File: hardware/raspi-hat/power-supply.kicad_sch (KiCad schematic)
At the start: 3 parts, among them J3 ATX-20, J4 Raspberry_Pi_4

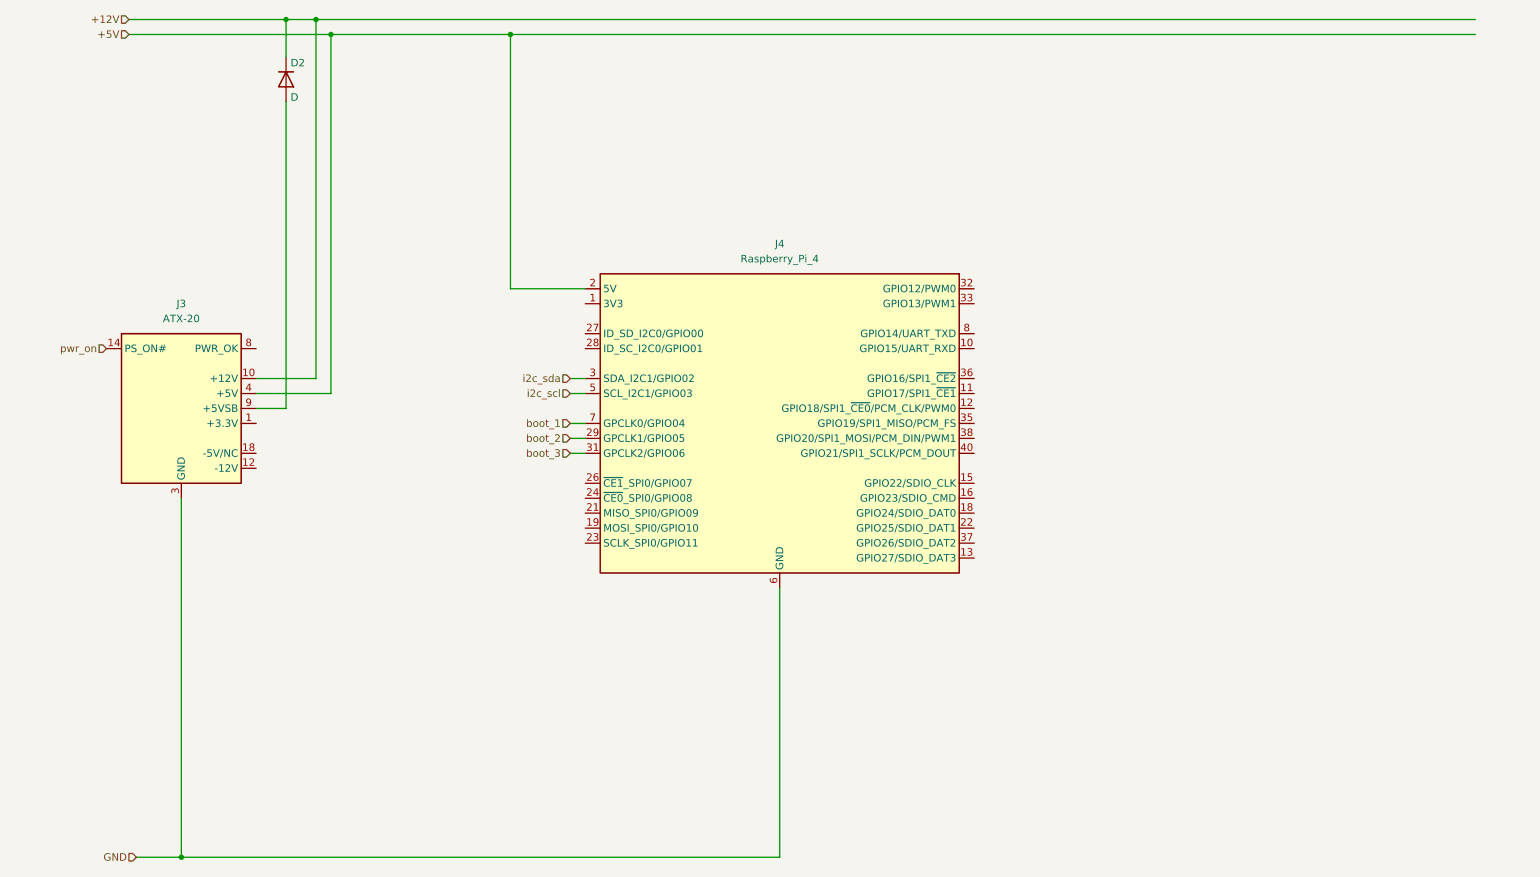
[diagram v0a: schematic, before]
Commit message: - added some lines on hardwaer - added libmotor as dependency
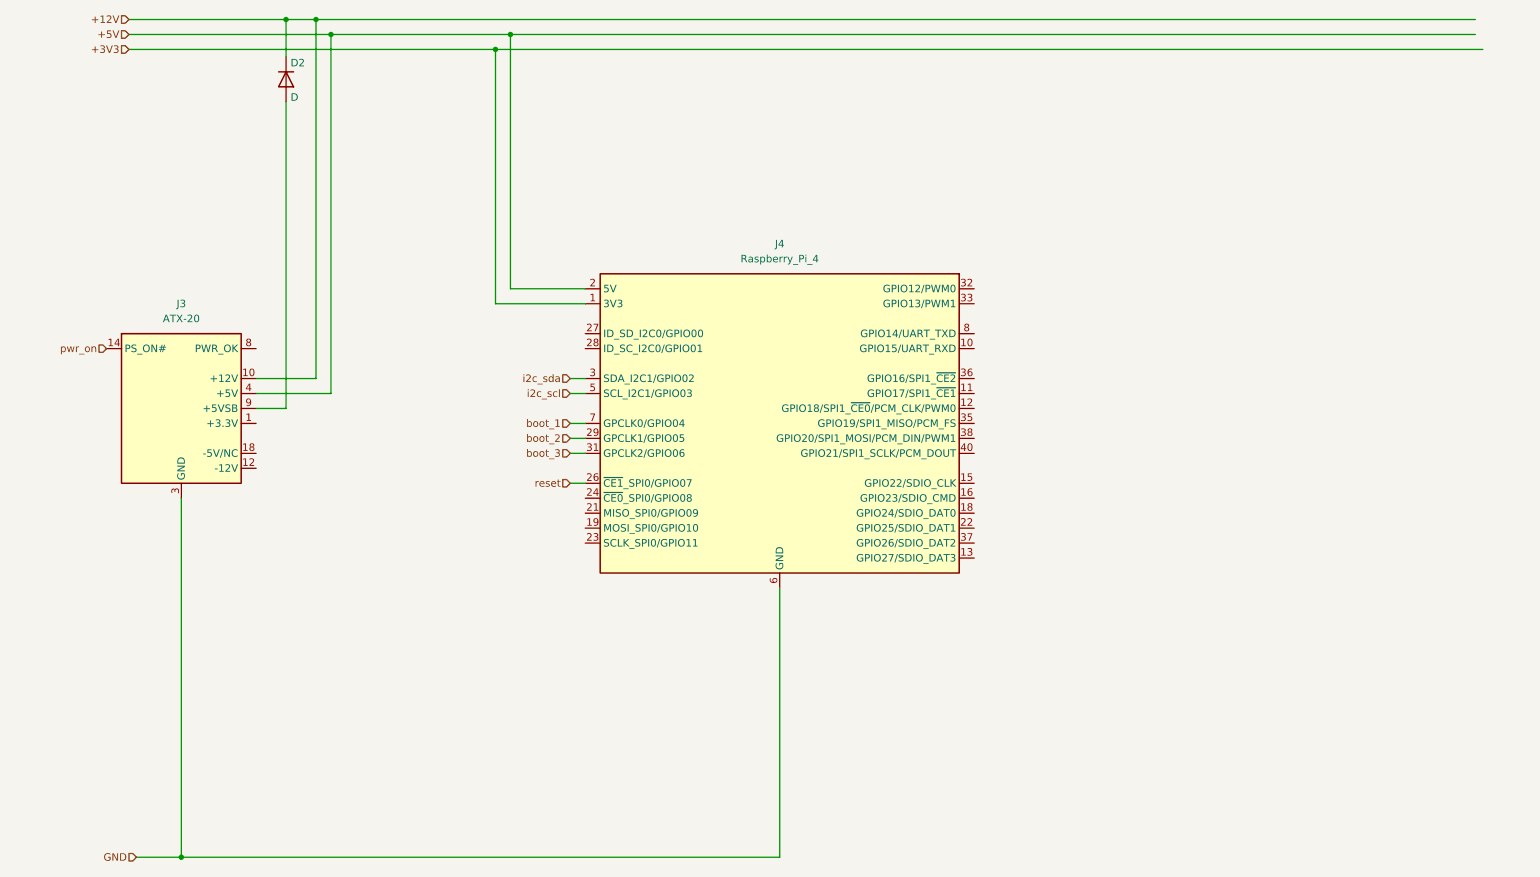
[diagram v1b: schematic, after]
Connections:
- net +3V3: now reaches J4.1 (3V3), J4.17 (3V3)
- net reset: now reaches J4.26 (~{CE1}_SPI0/GPIO07)
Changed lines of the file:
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@@
+	)
+	(junction
+		(at 102.87 30.48)
+		(diameter 0)
+		(color 0 0 0 0)
 	)
 	(junction
@@
 	(wire
 		(pts
+			(xy 40.64 30.48) (xy 102.87 30.48)
+		)
+		(stroke
+			(width 0)
+			(type default)
+		)
+	)
+	(wire
+		(pts
 			(xy 67.31 25.4) (xy 67.31 31.75)
 		)
@@
 	(wire
 		(pts
+			(xy 102.87 30.48) (xy 270.51 30.48)
+		)
+		(stroke
+			(width 0)
+			(type default)
+		)
+	)
+	(wire
+		(pts
 			(xy 72.39 25.4) (xy 269.24 25.4)
 		)
@@
 	(wire
 		(pts
+			(xy 115.57 104.14) (xy 118.11 104.14)
+		)
+		(stroke
+			(width 0)
+			(type default)
+		)
+	)
+	(wire
+		(pts
+			(xy 102.87 30.48) (xy 102.87 73.66)
+		)
+		(stroke
+			(width 0)
+			(type default)
+		)
+	)
+	(wire
+		(pts
 			(xy 115.57 86.36) (xy 118.11 86.36)
 		)
@@
 	(wire
 		(pts
+			(xy 118.11 73.66) (xy 102.87 73.66)
+		)
+		(stroke
+			(width 0)
+			(type default)
+		)
+	)
+	(wire
+		(pts
 			(xy 72.39 86.36) (xy 72.39 25.4)
 		)
@@
 		)
 	)
+	(hierarchical_label "+3V3"
+		(shape input)
+		(at 40.64 30.48 180)
+		(effects
+			(font
+				(size 1.27 1.27)
+			)
+			(justify right)
+		)
+	)
 	(hierarchical_label "boot_2"
 		(shape input)
@@
 		(effects
 			(font
+				(size 1.27 1.27)
+			)
+			(justify right)
+		)
+	)
+	(hierarchical_label "reset"
+		(shape input)
+		(at 115.57 104.14 180)
+		(effects
+			(font

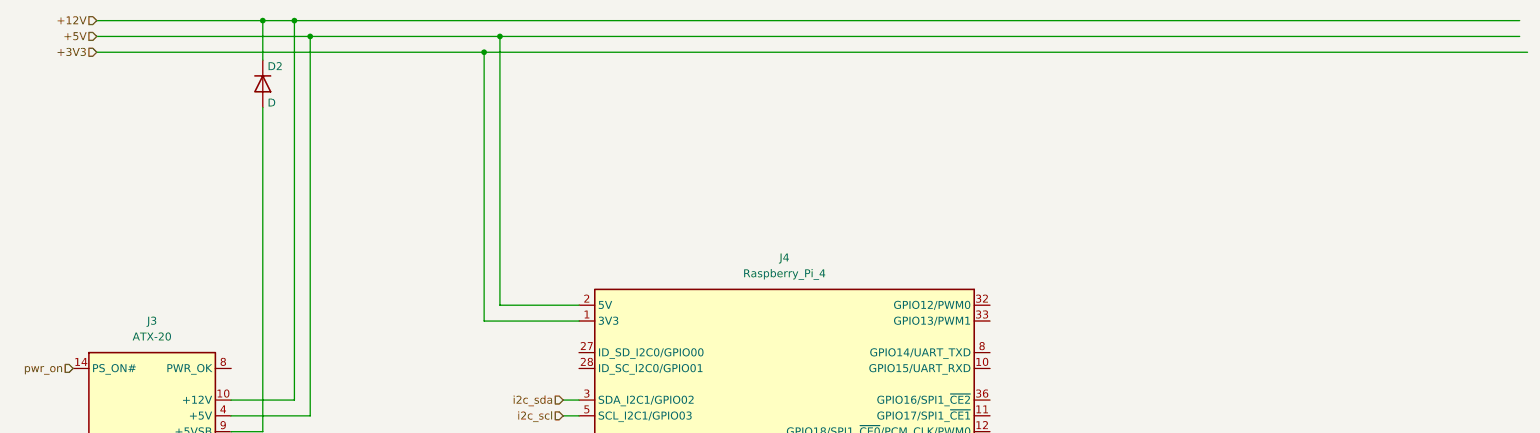
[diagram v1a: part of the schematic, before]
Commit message: added op amp parts to pcb
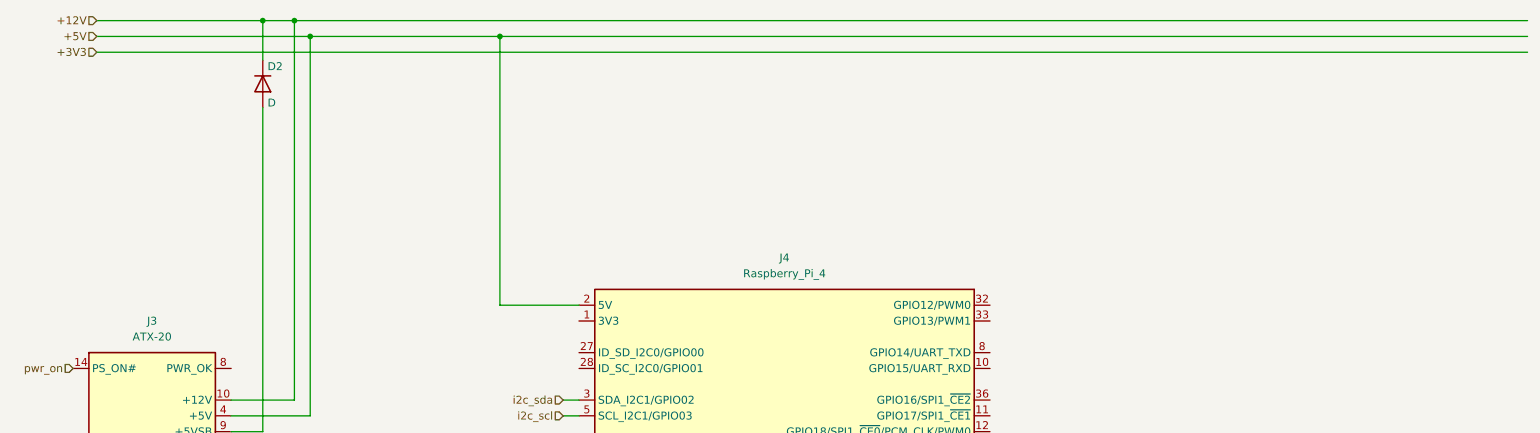
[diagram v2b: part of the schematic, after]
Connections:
- net +3V3: no longer J4.1 (3V3), J4.17 (3V3)
- new net: J4.1 (3V3), J4.17 (3V3)
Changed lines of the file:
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@@
-	)
-	(junction
-		(at 102.87 30.48)
-		(diameter 0)
-		(color 0 0 0 0)
 	)
 	(junction
@@
 	(wire
 		(pts
-			(xy 40.64 30.48) (xy 102.87 30.48)
-		)
-		(stroke
-			(width 0)
-			(type default)
-		)
-	)
-	(wire
-		(pts
 			(xy 67.31 25.4) (xy 67.31 31.75)
 		)
@@
 	(wire
 		(pts
-			(xy 102.87 30.48) (xy 270.51 30.48)
-		)
-		(stroke
-			(width 0)
-			(type default)
-		)
-	)
-	(wire
-		(pts
-			(xy 72.39 25.4) (xy 269.24 25.4)
+			(xy 40.64 30.48) (xy 270.51 30.48)
+		)
+		(stroke
+			(width 0)
+			(type default)
+		)
+	)
+	(wire
+		(pts
+			(xy 72.39 25.4) (xy 270.51 25.4)
 		)
 		(stroke
@@
 	(wire
 		(pts
-			(xy 105.41 27.94) (xy 269.24 27.94)
+			(xy 105.41 27.94) (xy 270.51 27.94)
 		)
 		(stroke
@@
 	(wire
 		(pts
-			(xy 102.87 30.48) (xy 102.87 73.66)
-		)
-		(stroke
-			(width 0)
-			(type default)
-		)
-	)
-	(wire
-		(pts
 			(xy 115.57 86.36) (xy 118.11 86.36)
 		)
@@
 		)
 		(stroke
-			(width 0)
-			(type default)
-		)
-	)
-	(wire
-		(pts
-			(xy 118.11 73.66) (xy 102.87 73.66)
-		)
-		(stroke

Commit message: updatd ioc
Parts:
- removed D2: D, symbol Device:D
- added D3: ER1Q-LTP, Diode_SMD:D_SMB, symbol Device:D
- added R23, R24: 0, Resistor_SMD:R_0603_1608Metric, symbol Device:R
- J4: footprint (none) -> Connector_PinSocket_2.54mm:PinSocket_2x20_P2.54mm_Vertical
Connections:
- net +12V: now also D3.1 (K)
- net +3V3: now also R23.2, R24.2
- net at J3.9 (+5VSB): now also D3.2 (A)
- net at J3.1 (+3.3V), J3.11 (+3.3V), J3.2 (+3.3V): now also R24.1
- net at J4.1 (3V3), J4.17 (3V3): now also R23.1
- net uart_rx: now reaches J4.10 (GPIO15/UART_RXD)
- net uart_tx: now reaches J4.8 (GPIO14/UART_TXD)
- net boot_1 renamed boot
- net boot_2: no longer names the net of J4.29 (GPCLK1/GPIO05)
- net boot_3: no longer names the net of J4.31 (GPCLK2/GPIO06)
